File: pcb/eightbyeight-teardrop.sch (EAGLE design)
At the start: 164 parts, among them CON1 USB_MICROSMT+THRUHULE, Q1 16MHz, SW1 SWITCH_SPDT, SW2 BRIGHTNESS, U1 MK20DN64VFM5, U10 FDG6316P, U11 FDG6316P, U12 FDG6316P, U2 ICN2026, U3 74138, U4 ICN2026, U5 MIC5219 3.3V, U6 ESP_WROOM_02, U8 MMA8653FC, U9 FDG6316P

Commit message: Rev E, as submitted
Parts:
- removed 16, 3.3V, 5, ANALOG_IN, GROUND: PTR1B2,54, testpad:PTR1B2,54
- added U$10, U$2, U$6, U$9: TEST_POINT, DevicesToMerge:TEST_POINT
- R1: value 2k 1% -> 1.6k 1%
- R12, R21, R23, R25, R26, R27, R6: value 47k -> 10k
- R13, R14, R15, R16, R2, R3, R4, R5: value 2k -> 4.7k
- renumbered BAT to J2, CON1 to J1, U$8 to U7
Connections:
- net +3V3: now also U$10.P$1; no longer 3.3V.TP
- net ESP_GPIO16: now also U$9.P$1; no longer 16.TP
- net ESP_TOUT: no longer ANALOG_IN.TP
- net EXP_GPIO5: now also U$6.P$1; no longer 5.TP
- net GND: now also U$2.P$1; no longer GROUND.TP
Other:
- note added: "ESP826 Boot Select UART Download: GPIO15 Low, GPIO0 Low, GPIO2 High Flash Boot: GPIO15 Low, GPIO0 Hight, GPIO2 High Note: The ESP8266 needs strong pullup/down resistors on the boot select lines. 10k is stable, 47k is marginal, and 100k is unreliable."
- note removed: "ESP826 Boot Select UART Download: GPIO15 Low, GPIO0 Low, GPIO2 High Flash Boot: GPIO15 Low, GPIO0 Hight, GPIO2 High"
- moved on the sheet: R12, R23, R25

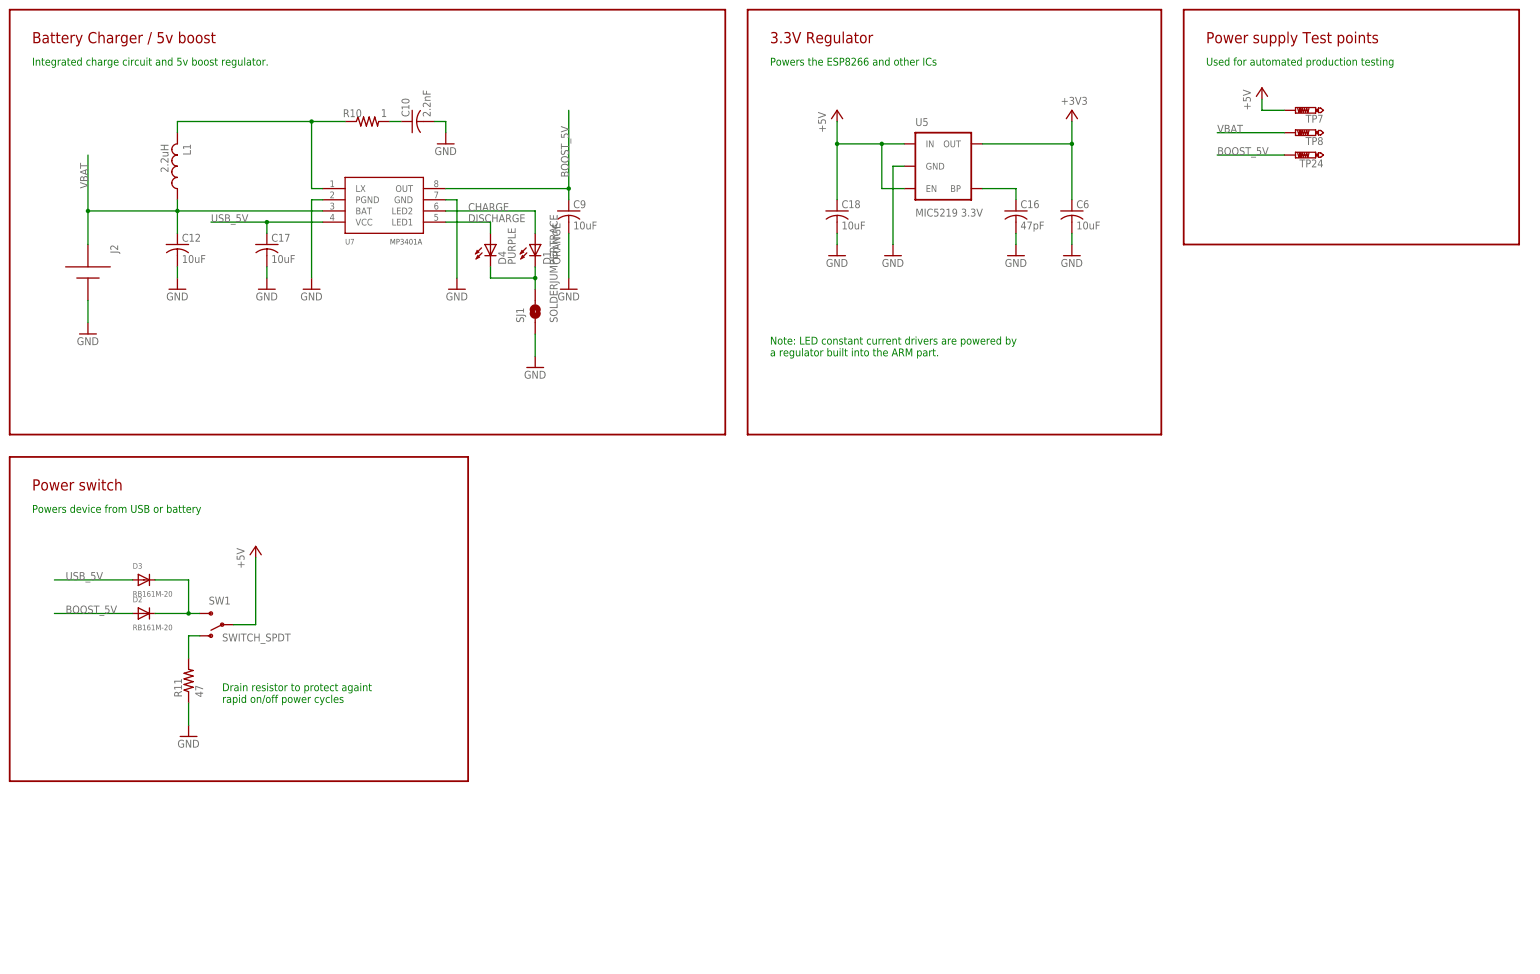
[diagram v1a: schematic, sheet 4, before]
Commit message: Add seperate bleed resistor to 5V input
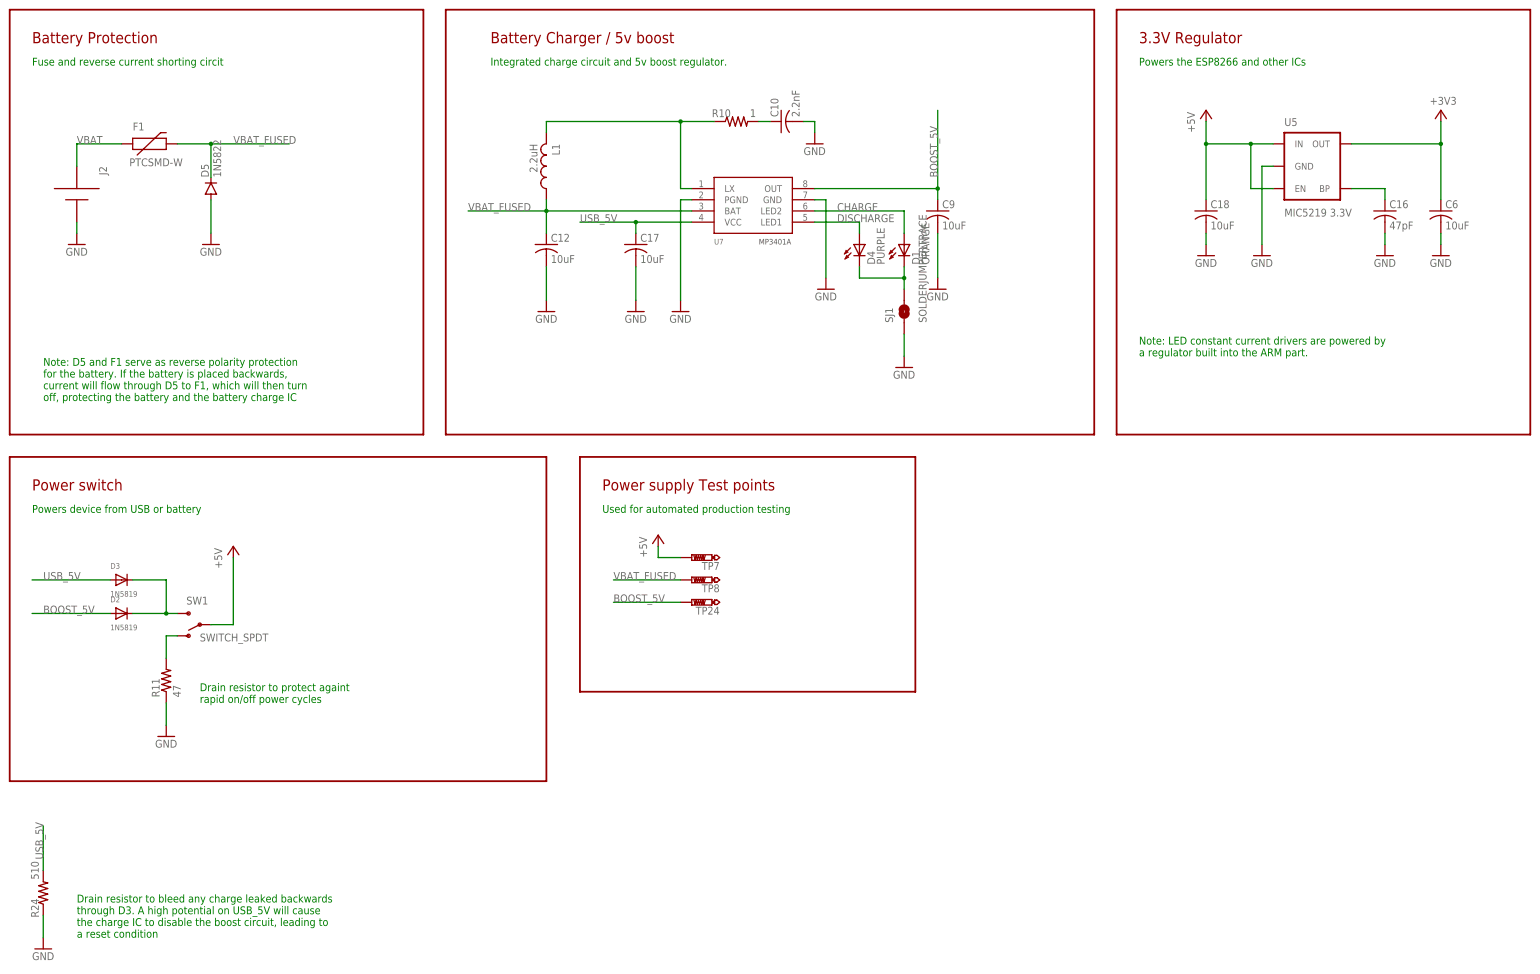
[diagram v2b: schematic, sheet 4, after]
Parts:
- added D5: 1N5822, SparkFun-DiscreteSemi:DIODESMA
- added F1: PTCSMD-W, SparkFun-PowerIC:PTCSMD-W
- added R24: 510, adafruit:R-US_R0603
- D2, D3: value RB161M-20 -> 1N5819
- R1: value 1.6k 1% -> 1k 1%
- R28: value DNP -> 10k
- R9: value 2k 1% -> 1k 1%
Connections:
- new net VBAT_FUSED: C12.1, D5.C, F1.2, L1.1, TP8.TP, U7.BAT
- net GND: now also D5.A, R24.1
- net USB_5V: now also R24.2
- net VBAT: now also F1.1; no longer C12.1, L1.1, TP8.TP, U7.BAT
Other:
- note added: "Battery Protection"
- note added: "Drain resistor to bleed any charge leaked backwards through D3. A high potential on USB_5V will cause the charge IC to disable the boost circuit, leading to a reset condition"
- note added: "Fuse and reverse current shorting circit"
- note added: "Note: D5 and F1 serve as reverse polarity protection for the battery. If the battery is placed backwards, current will flow through D5 to F1, which will then turn off, protecting the battery and the battery charge IC"
- note added: "Pin assignments for matrix output: LED_DAT + LED_CLK use ESPI hardware LED_OE and LED_STB need to be on pins with FTM0 capability LED_ROW_* are GPIO and need to be together on a unique port"
- note added: "This documentation describes Open Hardware and is licensed under the CERN OHL v. 1.2. You may redistribute and modify this documentation under the terms of the CERN OHL v.1.2. (http://ohwr.org/cernohl). This documentation is distributed WITHOUT ANY EXPRESS OR IMPLIED WARRANTY, INCLUDING OF MERCHANTABILITY, SATISFACTORY QUALITY AND FITNESS FOR A PARTICULAR PURPOSE. Please see the CERN OHL v.1.2 fo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"
- note removed: "Pin assignments for matrix output: LED_DAT + LED_CLK use ESPI hardware LED_OE needs to be on a pin with FTM capability LED_ROW_* and LED_STB are GPIO and need to be together on a unique port"
- moved on the sheet: C10, C12, C16, C17, C18, C6, C9, D1, D2, D3, D4, J2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

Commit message: Teardrop trial before release
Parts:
- C1, C11, C13, C14, C15, C16, C2, C3, C4, C5, C7, C8: device adafruit:C-USC0402 -> blinkinlabs:C_US0402
- C10: device adafruit:C-USC0603 -> blinkinlabs:C_US0603
- C12, C17, C18, C6, C9: device adafruit:C-USC0805 -> blinkinlabs:C_US0805
- D2, D3: device adafruit:DIODESOD-123 -> blinkinlabs:DIODESOD-123
- J2: value BATTERY -> BATTERYAA_SMD; device blinkinlabs:BATTERY -> blinkinlabs:BATTERYAA_SMD
- LED_1, LED_10, LED_11, LED_12, LED_13, LED_14, LED_15, LED_16, LED_17, LED_18, LED_19, LED_2, LED_20, LED_21, LED_22, LED_23, LED_24, LED_25, LED_26, LED_27, LED_28, LED_29, LED_3, LED_30, LED_31, LED_32, LED_33, LED_34, LED_35, LED_36, LED_37, LED_38, LED_39, LED_4, LED_40, LED_41, LED_42, LED_43, LED_44, LED_45, LED_46, LED_47, LED_48, LED_49, LED_5, LED_50, LED_51, LED_52, LED_53, LED_54, LED_55, LED_56, LED_57, LED_58, LED_59, LED_6, LED_60, LED_61, LED_62, LED_63, LED_64, LED_7, LED_8, LED_9: value LED_RGB_CA -> LED_RGB_CA3528; device blinkinlabs:LED_RGB_CA -> blinkinlabs:LED_RGB_CA3528
- R1, R12, R13, R14, R15, R16, R17, R18, R2, R21, R23, R25, R26, R27, R28, R3, R4, R5, R6, R7, R8, R9: device adafruit:R-US_R0402 -> blinkinlabs:R_US0402
- R10, R24: device adafruit:R-US_R0603 -> blinkinlabs:R_US0603
- R11: device adafruit:R-US_R0805 -> blinkinlabs:R_US0805
- SW2: device blinkinlabs:BUTTON_MOMENTARY_GROUND -> blinkinlabs:BUTTON_MOMENTARY_GROUNDTD-07XB
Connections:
- net ESP_GPIO16: now also U6.IO16; no longer U6.IO18
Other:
- note added: "Note: The reverse current leakage of the diodes is a critical spec. The leakage should be <50uA at 5V and operating temperature."
- moved on the sheet: D2, D3, R11, SW1

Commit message: Switch to larger PTC, release RevH
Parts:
- removed F1: PTCSMD-W, SparkFun-PowerIC:PTCSMD-W
- added L2: 1812L260THDR, rcl:L-EUL1812
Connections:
- net VBAT: now also L2.1; no longer F1.1
- net VBAT_FUSED: now also L2.2; no longer F1.2
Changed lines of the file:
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@@
 <part name="D5" library="SparkFun-DiscreteSemi" deviceset="DIODE" device="SMA" value="1N5822"/>
 <part name="GND47" library="SparkFun-Aesthetics" deviceset="GND" device=""/>
-<part name="F1" library="SparkFun-PowerIC" deviceset="PTC" device="SMD-W" value="PTCSMD-W"/>
 <part name="GND48" library="SparkFun-Aesthetics" deviceset="GND" device=""/>
 <part name="R24" library="blinkinlabs" deviceset="R_US" device="0603" value="510"/>
+<part name="L2" library="rcl" deviceset="L-EU" device="L1812" value="1812L260THDR"/>
 </parts>
 <sheets>
@@
 <instance part="D5" gate="G$1" x="53.34" y="210.82" rot="R90"/>
 <instance part="GND47" gate="1" x="53.34" y="198.12"/>
-<instance part="F1" gate="G$1" x="38.1" y="220.98"/>
 <instance part="GND48" gate="1" x="15.24" y="38.1"/>
 <instance part="R24" gate="G$1" x="15.24" y="50.8" smashed="yes" rot="R90">
@@
 <attribute name="VALUE" x="14.224" y="53.848" size="1.778" layer="96" rot="R90"/>
 </instance>
+<instance part="L2" gate="G$1" x="40.64" y="220.98" rot="R90"/>
 </instances>
 <busses>
@@
 <segment>
 <label x="58.42" y="220.98" size="1.778" layer="95"/>
-<wire x1="45.72" y1="220.98" x2="53.34" y2="220.98" width="0.1524" layer="91"/>
 <pinref part="D5" gate="G$1" pin="C"/>
 <wire x1="53.34" y1="220.98" x2="71.12" y2="220.98" width="0.1524" layer="91"/>
 <wire x1="53.34" y1="213.36" x2="53.34" y2="220.98" width="0.1524" layer="91"/>
-<pinref part="F1" gate="G$1" pin="2"/>
 <junction x="53.34" y="220.98"/>
+<pinref part="L2" gate="G$1" pin="2"/>
+<wire x1="53.34" y1="220.98" x2="45.72" y2="220.98" width="0.1524" layer="91"/>
 </segment>
 <segment>
@@
 <segment>
 <pinref part="J2" gate="G$1" pin="+"/>
-<pinref part="F1" gate="G$1" pin="1"/>
-<wire x1="33.02" y1="220.98" x2="22.86" y2="220.98" width="0.1524" layer="91"/>
+<label x="22.86" y="220.98" size="1.778" layer="95" rot="R90"/>
+<pinref part="L2" gate="G$1" pin="1"/>
+<wire x1="35.56" y1="220.98" x2="22.86" y2="220.98" width="0.1524" layer="91"/>
 <wire x1="22.86" y1="220.98" x2="22.86" y2="215.9" width="0.1524" layer="91"/>
-<label x="22.86" y="220.98" size="1.778" layer="95"/>
-</segment>
-</net>
+</segment>
+</net>
